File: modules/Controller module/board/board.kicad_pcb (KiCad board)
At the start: 2 copper layers, 50 x 30 mm, 56 parts, among them IC1 DW01A, J1 Conn_01x04_Female, J2 Conn_01x04_Female, J3 Conn_01x05_Female, J4 Conn_01x02, J5 Conn_01x06_Female, J6 Conn_01x02_Female, P1 USB_C_Plug_USB2.0, Q1 AO3400A, Q2 AO3400A, Q3 AO3401A, Q4 FS8205A, SW1 SW_Push, SW2 SW_SPST, SW3 SW_Push, U1 ME6211, U2 ESP32-WROOM-32D, U3 Inertial_Measurement_Unit, U4 TP4056

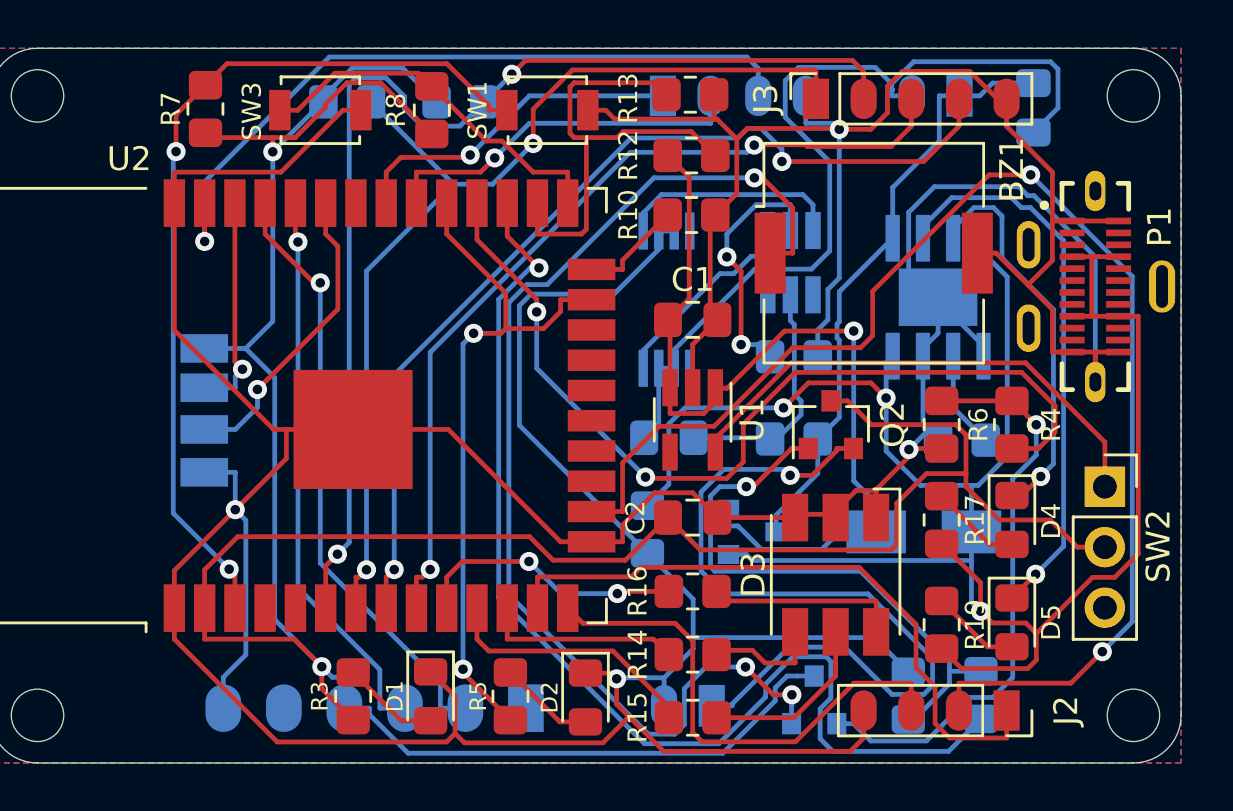
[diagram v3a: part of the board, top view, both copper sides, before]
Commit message: PCB: IMU
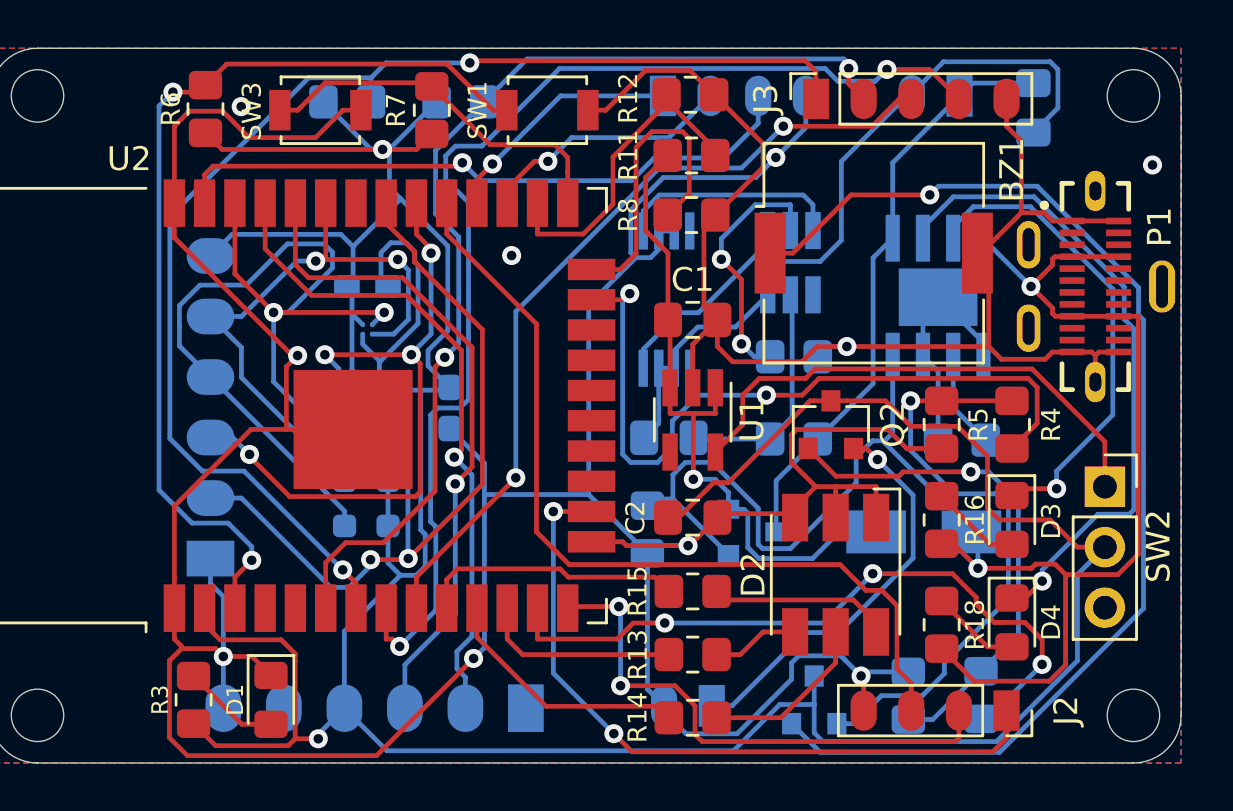
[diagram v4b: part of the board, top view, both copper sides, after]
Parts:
- removed the D2 at (130.0, 113.2)
- removed the R5 at (126.8, 113.2)
- removed the U3 at (121.5, 101.1)
- added C5: 100nF, Capacitor_SMD:C_0603_1608Metric_Pad1.08x0.95mm_HandSolder, B.Cu at (124.3, 101.1)
- added C6: 2.2uF, Capacitor_SMD:C_0603_1608Metric_Pad1.08x0.95mm_HandSolder, B.Cu at (120.8, 96.0)
- added J7: Conn_01x06_Male, Board:SolderWire_1x06_P2.54mm, B.Cu at (114.3, 107.4)
- added R22: 10k, Resistor_SMD:R_0603_1608Metric_Pad0.98x0.95mm_HandSolder, B.Cu at (120.8, 104.2)
- added R23: 10k, Resistor_SMD:R_0603_1608Metric_Pad0.98x0.95mm_HandSolder, B.Cu at (120.8, 106.0)
- added U4: ASM330LHHXTR, Board:ASM330LHHXTR, B.Cu at (120.8, 101.1)
- added U5: MMC5603NJ, Board:MMC5603NJ, B.Cu at (120.8, 97.8)
- moved D1 6.70 mm to (116.8, 113.3)
- moved R3 6.70 mm to (113.5, 113.3)
- renumbered D3 to D2, D4 to D3, D5 to D4, D6 to D5, R11 to R10, R12 to R11, R13 to R12, R14 to R13, R15 to R14, R16 to R15, R17 to R16, R18 to R17, R19 to R18, R20 to R19, R21 to R20, R22 to R21, R6 to R5, R7 to R6, R8 to R7, R10 to R8, U4 to U3
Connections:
- R9 pad 2: /IO16 -> /IO14
- U2 pad 13: /BTN-T -> /IO14
- U2 pad 14: /BTN-R -> /BTN-M
- U2 pad 16: /BTN-M -> /BTN-T
- U2 pad 23: /IO15 -> /BUZZER
- U2 pad 27: /IO16 -> /BTN-B
- U2 pad 28: /BUZZER -> /BTN-A
- U2 pad 29: /IO15 -> /BTN-R
- U2 pad 30: /BTN-B -> INT1
- U2 pad 31: /BTN-A -> INT2
- U2 pad 33: /IO21 -> SCL
- U2 pad 36: /IO22 -> SDA
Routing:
- net /IO16: track 47.4 -> 0.00 mm, vias 1 -> 0
- net SDA: track 0.00 -> 42.5 mm, vias 0 -> 2
- net INT2: track 0.00 -> 35.5 mm, vias 0 -> 2
- net /BTN-M: track 56.6 -> 22.6 mm
- net /IO14: track 0.00 -> 29.7 mm, vias 0 -> 3
- net /IO15: track 29.4 -> 0.00 mm, vias 2 -> 0
- net INT1: track 0.00 -> 28.3 mm, vias 0 -> 4
- net SCL: track 0.00 -> 27.5 mm, vias 0 -> 2
- net Net-(J4-Pad1): track 34.4 -> 17.0 mm
- net +3V3: track 134.0 -> 150.2 mm
- net /BTN-R: track 21.2 -> 36.4 mm
- net /IO21: track 12.8 -> 0.00 mm, vias 1 -> 0
- net +5V: track 84.2 -> 72.2 mm, vias 3 -> 2
- net VCC: track 37.5 -> 28.1 mm
- net GND: track 255.4 -> 246.0 mm, vias 4 -> 10
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
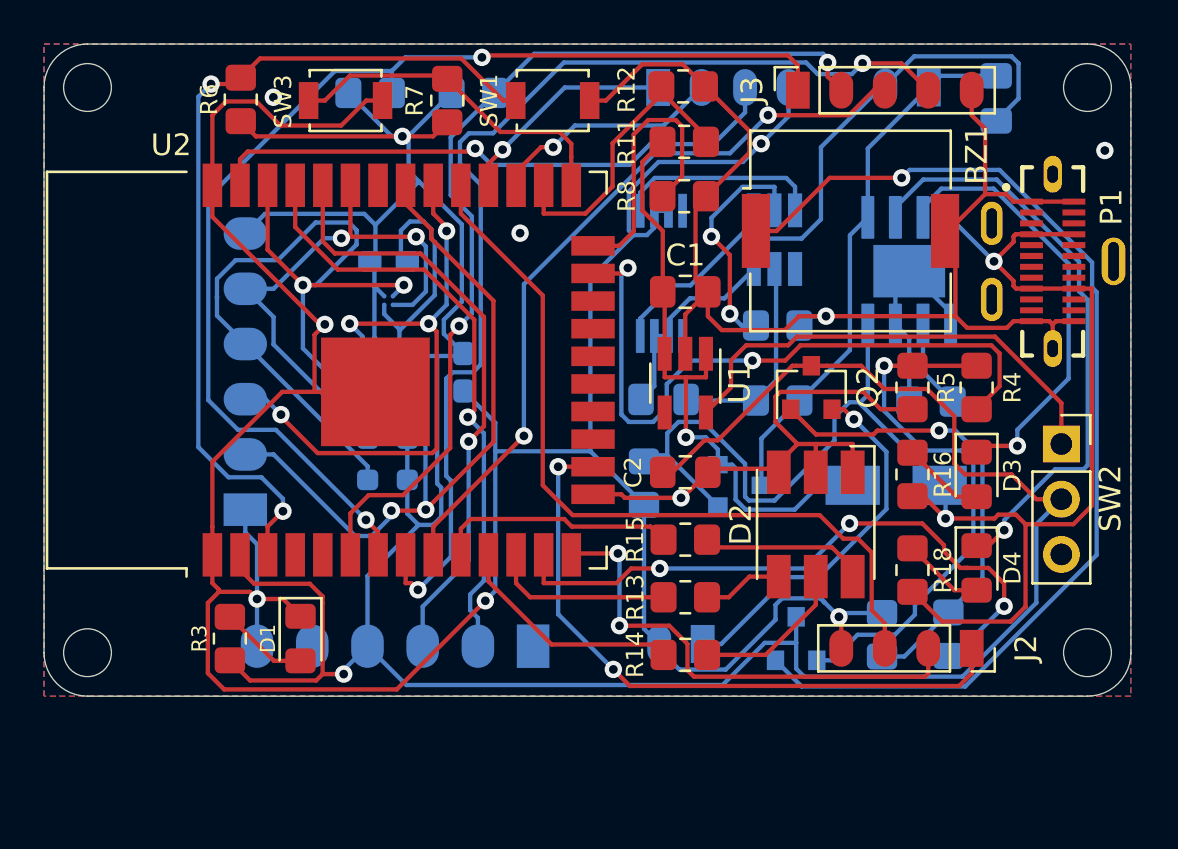
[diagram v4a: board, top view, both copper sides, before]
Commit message: Controller module: Optical Flow Sensor Connector
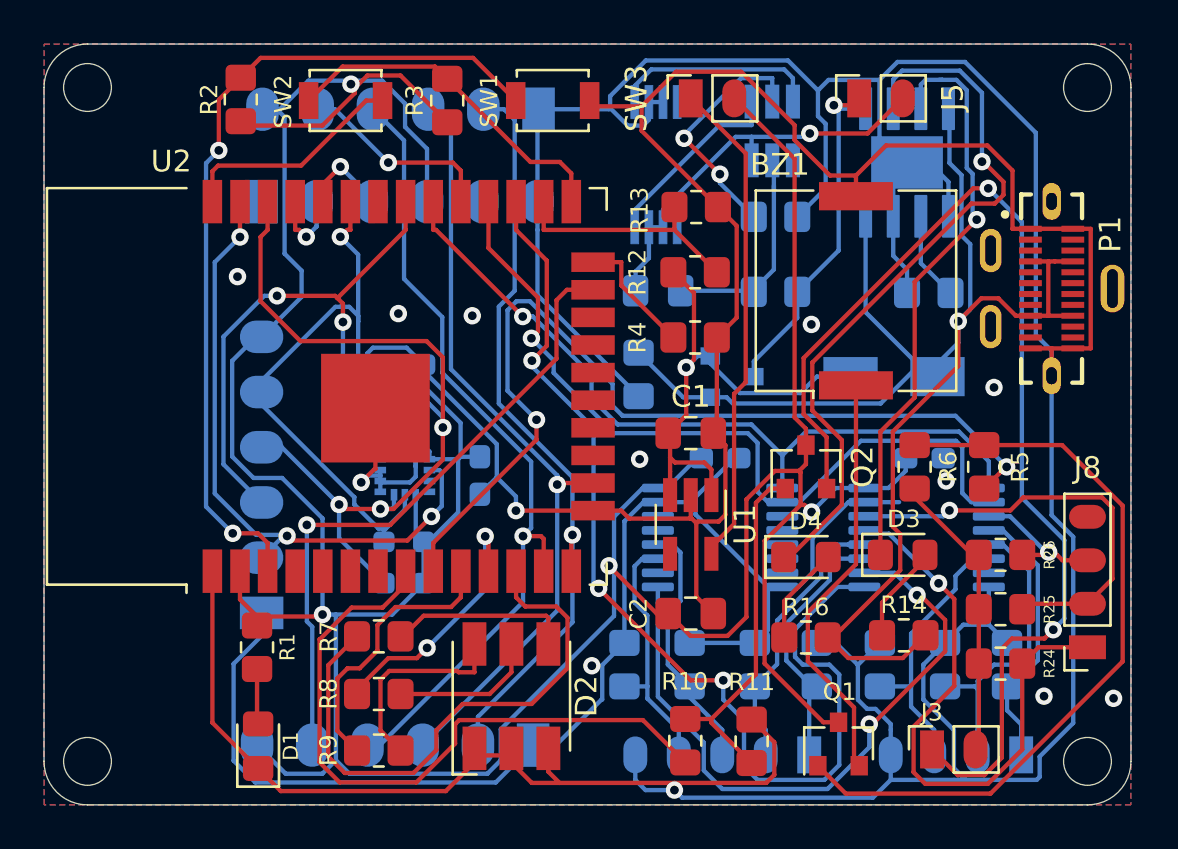
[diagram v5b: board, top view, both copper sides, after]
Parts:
- removed the C4 at (148.8, 88.5)
- removed the J3 at (139.7, 88.1)
- removed the R1 at (120.0, 88.2)
- removed the R2 at (124.8, 88.2)
- added C6: 0.1uF, Capacitor_SMD:C_0603_1608Metric_Pad1.08x0.95mm_HandSolder, B.Cu at (145.5, 105.0)
- added C7: 0.1uF, Capacitor_SMD:C_0603_1608Metric_Pad1.08x0.95mm_HandSolder, B.Cu at (136.1, 105.0)
- added J7: Conn_01x05_Female, Board:SolderWire_1x05_P2.00mm, B.Cu at (140.2, 118.7)
- added J8: Conn_01x04_Female, Board:SolderWire_1x04_P2.00mm, F.Cu at (153.0, 113.8)
- added J9: Conn_01x04_Female, Board:SolderWire_1x04_P2.00mm, B.Cu at (149.9, 118.7)
- added R22: 10k, Resistor_SMD:R_0805_2012Metric_Pad1.20x1.40mm_HandSolder, B.Cu at (140.6, 114.5)
- added R23: 10k, Resistor_SMD:R_0805_2012Metric_Pad1.20x1.40mm_HandSolder, B.Cu at (137.7, 114.5)
- added R24: 10k, Resistor_SMD:R_0805_2012Metric_Pad1.20x1.40mm_HandSolder, F.Cu at (149.0, 114.5)
- added R25: 10k, Resistor_SMD:R_0805_2012Metric_Pad1.20x1.40mm_HandSolder, F.Cu at (149.0, 112.0)
- added R26: 10k, Resistor_SMD:R_0805_2012Metric_Pad1.20x1.40mm_HandSolder, F.Cu at (149.0, 109.5)
- added R27: 10k, Resistor_SMD:R_0805_2012Metric_Pad1.20x1.40mm_HandSolder, B.Cu at (149.3, 114.5)
- added R28: 10k, Resistor_SMD:R_0805_2012Metric_Pad1.20x1.40mm_HandSolder, B.Cu at (146.4, 114.5)
- added R29: 10k, Resistor_SMD:R_0805_2012Metric_Pad1.20x1.40mm_HandSolder, B.Cu at (143.4, 114.5)
- added R30: 10k, Resistor_SMD:R_0805_2012Metric_Pad1.20x1.40mm_HandSolder, B.Cu at (131.7, 114.5)
- added R31: 10k, Resistor_SMD:R_0805_2012Metric_Pad1.20x1.40mm_HandSolder, B.Cu at (134.7, 114.5)
- added U6: 74HC165, Package_SO:TSSOP-16_4.4x5mm_P0.65mm, B.Cu at (145.6, 108.7)
- added U7: 74HC165, Package_SO:TSSOP-16_4.4x5mm_P0.65mm, B.Cu at (136.1, 108.7)
- J1: value Conn_01x04_Female -> Conn_01x06_Male; footprint Board:SolderWire_1x04_P2.00mm -> Board:SolderWire_1x06_P2.54mm
- J2: value Conn_01x04_Female -> Conn_01x06_Male; footprint Board:SolderWire_1x04_P2.00mm -> Board:SolderWire_1x06_P2.54mm; moved to B.Cu
- J3: renamed from J4; moved to F.Cu
- J5: renamed from J6; moved to F.Cu
- Q1: moved to F.Cu
- R10: renamed from R9; moved to F.Cu
- R11: renamed from R10; moved to F.Cu
- SW3: renamed from SW2; footprint Connector_PinSocket_2.54mm:PinSocket_1x03_P2.54mm_Vertical -> Board:SolderWire_1x02_P2.00mm
- moved J2 31.8 mm to (127.8, 89.0), turned to 90 degrees
- moved J1 30.8 mm to (127.5, 118.2), turned to 90 degrees
- moved J4 24.0 mm to (115.0, 93.2), turned to 270 degrees
- moved SW3 23.3 mm to (134.8, 88.5), turned to 90 degrees
- moved R9 17.1 mm to (120.4, 118.5)
- moved D2 16.1 mm to (126.5, 116.0), turned to 90 degrees
- moved R7 14.2 mm to (120.4, 113.2)
- moved R8 14.2 mm to (120.4, 115.9)
- moved R10 13.1 mm to (134.5, 118.0)
- moved J3 11.6 mm to (145.8, 118.5)
- moved D4 7.87 mm to (140.1, 109.6), turned to 0 degrees
- moved R11 7.75 mm to (137.6, 118.1)
- moved R14 7.41 mm to (144.6, 113.2), turned to 180 degrees
- moved R4 6.52 mm to (134.9, 99.5)
- moved C1 6.50 mm to (134.8, 103.9)
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- renumbered C5 to C4, C6 to C5, J5 to J4, J7 to J6, R3 to R1, R11 to R12, R12 to R13, R16 to R14, R17 to R15, R18 to R16, R19 to R17, R20 to R18, R21 to R19, R6 to R2, R22 to R20, R23 to R21, R7 to R3, R8 to R4, R4 to R5, R5 to R6, R13 to R7, R14 to R8, R15 to R9, SW3 to SW2
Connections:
- J1 pad 1: /BTN-A -> GND
- J1 pad 2: /BTN-B -> /IO12
- J1 pad 3: /BTN-C -> /IO13
- J1 pad 4: GND -> /IO14
- J2 pad 1: /BTN-T -> GND
- J2 pad 2: /BTN-M -> /IO12
- J2 pad 3: /BTN-R -> /IO13
- J2 pad 4: GND -> /IO14
- R10 pad 2: /IO14 -> /IO32
- U2 pad 14: /BTN-M -> /IO12
- U2 pad 16: /BTN-T -> /IO13
- U2 pad 23: /BUZZER -> /CS_1
- U2 pad 27: /BTN-B -> DATA
- U2 pad 28: /BTN-A -> CLK
- U2 pad 29: /BTN-R -> /CS_2
- U2 pad 30: INT1 -> LATCH
- U2 pad 31: INT2 -> INT1
- U2 pad 37: /BTN-C -> INT2
- U2 pad 6: /BTN2 -> (no net)
- U2 pad 7: /BTN1 -> (no net)
- U2 pad 8: /BTN4 -> /IO32
- U2 pad 9: /BTN3 -> /BUZZER
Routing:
- net GND: track 246.0 -> 373.0 mm, vias 10 -> 13
- net /BTN1: track 52.9 -> 0.00 mm, vias 2 -> 0
- net /BTN4: track 49.0 -> 0.00 mm, vias 2 -> 0
- net DATA: track 0.00 -> 48.5 mm, vias 0 -> 3
- net /BTN2: track 43.6 -> 0.00 mm, vias 2 -> 0
- net CLK: track 0.00 -> 36.7 mm, vias 0 -> 1
- net /BTN-R: track 36.4 -> 0.00 mm
- net /IO13: track 0.00 -> 36.4 mm, vias 0 -> 1
- net /IO12: track 0.00 -> 35.6 mm, vias 0 -> 1
- net LATCH: track 0.00 -> 35.5 mm, vias 0 -> 1
- net Net-(J3-Pad1): track 17.0 -> 51.9 mm, vias 1 -> 2
- net /BTN3: track 34.5 -> 0.00 mm, vias 2 -> 0
- net /IO32: track 0.00 -> 31.0 mm
- net Net-(BZ1-Pad1): track 49.7 -> 19.4 mm, vias 1 -> 0
- net /BTN-T: track 30.2 -> 0.00 mm, vias 2 -> 0
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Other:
- board size 50 x 30 mm -> 50 x 35 mm
- board text removed: "InputBlackBoxOutput"
